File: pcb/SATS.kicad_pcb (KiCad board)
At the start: 2 copper layers, 108.5 x 103.4 mm, 27 parts, among them J1 Raspberry_Pi_2_3, J10 EXT_GPIO, J11 EXT_GPIO, J12 EXT_GPIO, J13 EXT_GPIO, J2 A00-432-262-450, J3 AudioJack4_SwitchTR1, J4 5V, J5 3.3V, J6 Card LED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

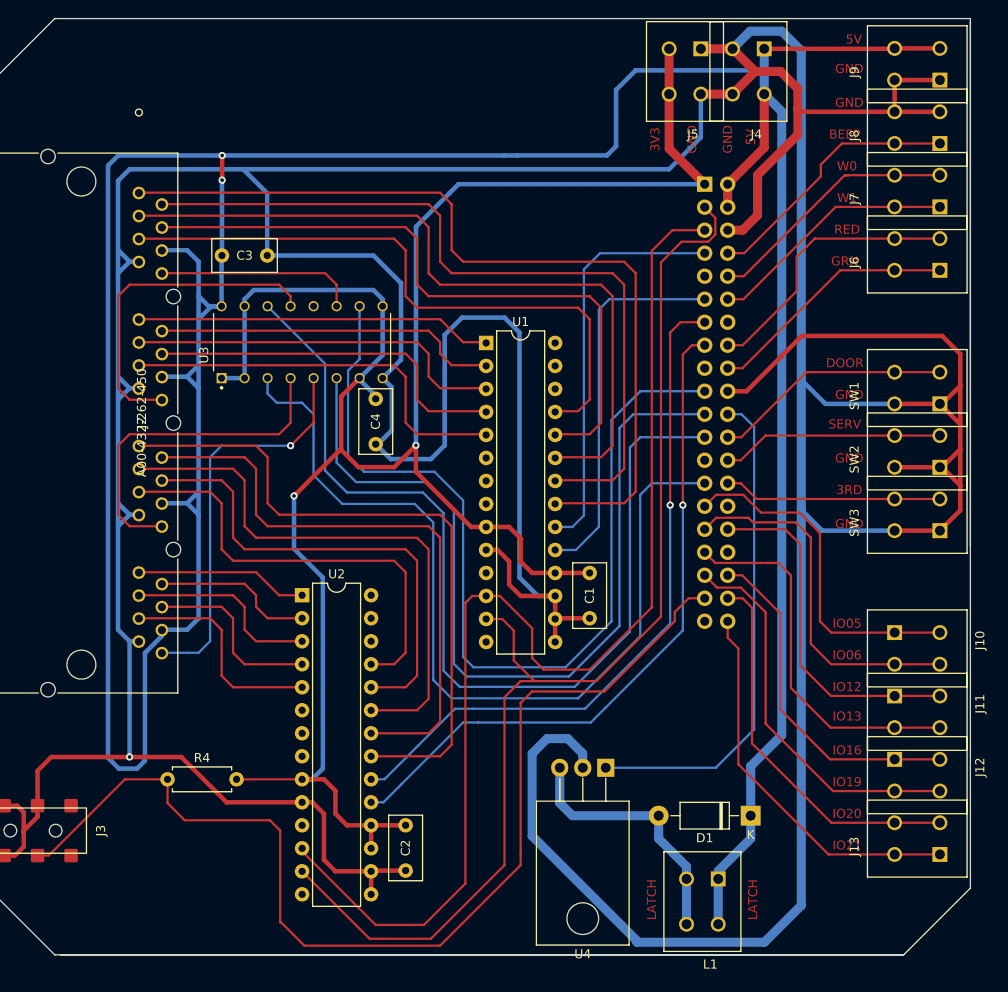
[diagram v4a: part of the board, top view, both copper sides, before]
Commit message: Clean Board Edge and Foottprints
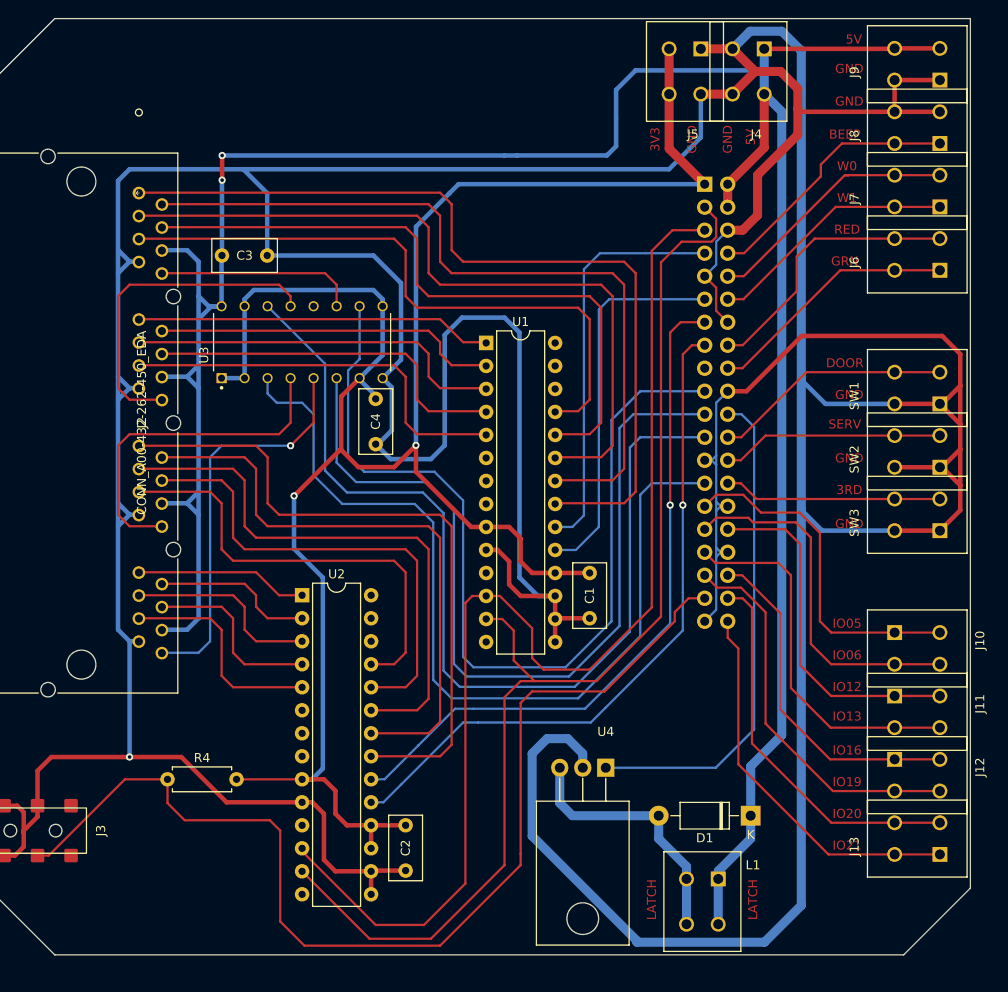
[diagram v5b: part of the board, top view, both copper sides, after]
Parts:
- J2: value A00-432-262-450 -> CONN_A00-432-262-450_EDA
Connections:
- J1 pad 17: +3V3 -> unconnected-(J1-Pad17)
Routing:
- net +5V: track 384.8 -> 286.2 mm
- net Earth: track 669.9 -> 715.2 mm
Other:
- outline, holes or cut-outs redrawn

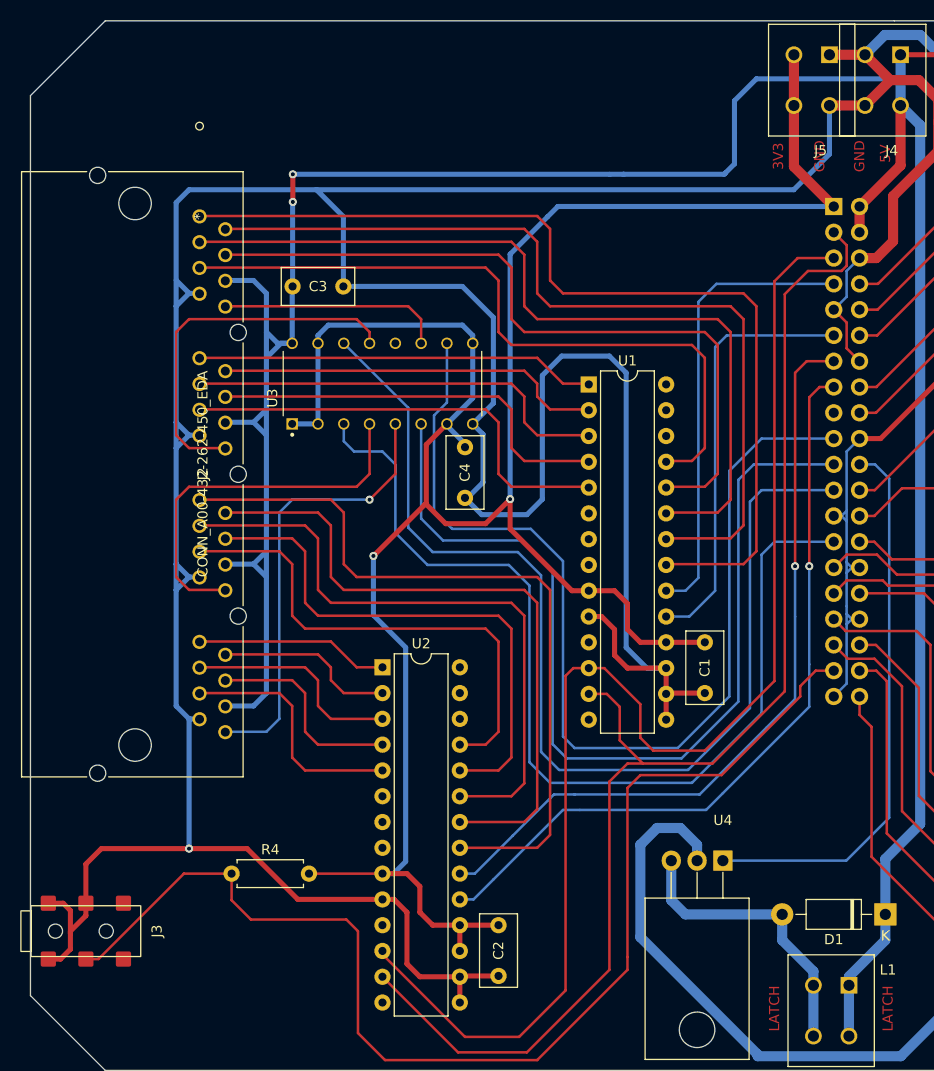
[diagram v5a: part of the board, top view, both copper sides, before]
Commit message: add copper labels
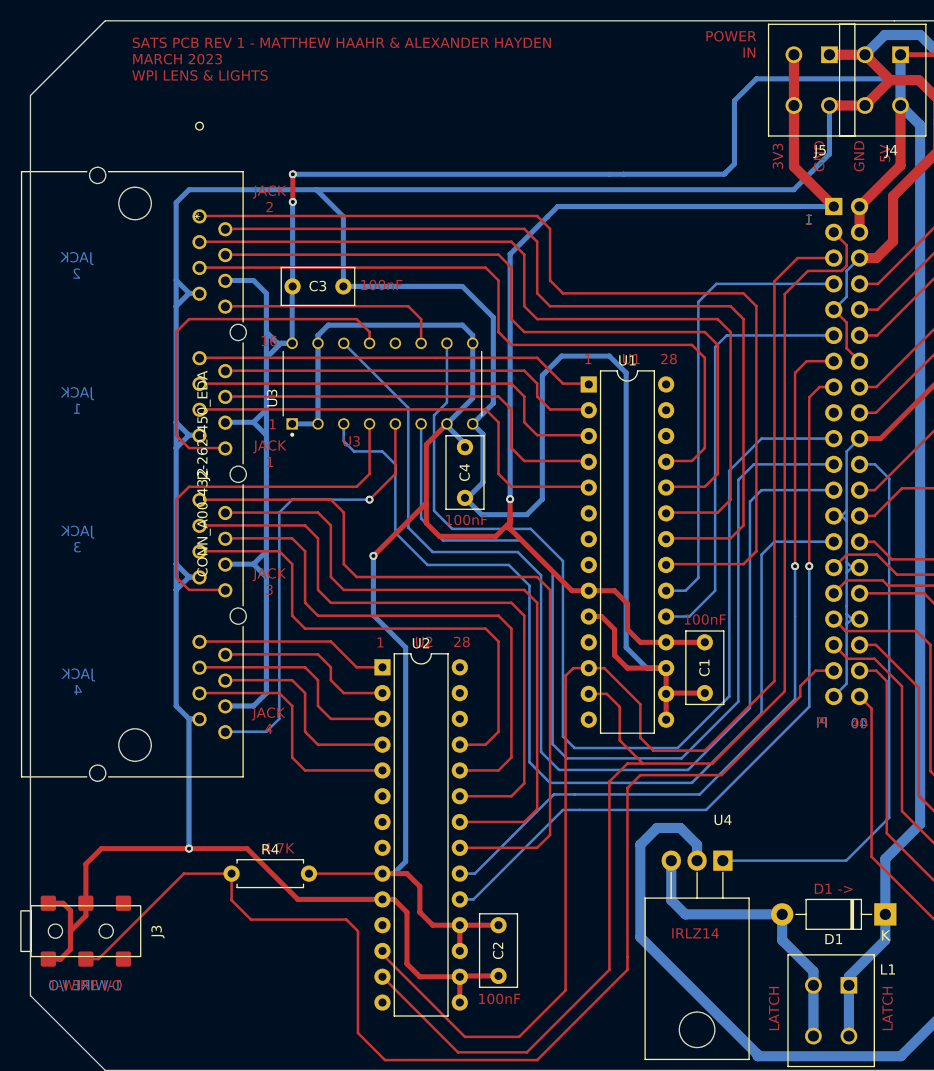
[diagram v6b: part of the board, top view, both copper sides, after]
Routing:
- net +3V3: track 228.0 -> 229.9 mm
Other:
- board text added: "1"
- board text added: "1-WIRE I/O"
- board text added: "100nF"
- board text added: "16"
- board text added: "28"
- board text added: "4.7K"
- board text added: "40"
- board text added: "D1 ->"
- board text added: "IRLZ14"
- board text added: "JACK 1"
- board text added: "JACK 2"
- board text added: "JACK 3"
- board text added: "JACK 4"
- board text added: "PI"
- board text added: "POWER IN"
- board text added: "SATS PCB REV 1 - MATTHEW HAAHR & ALEXANDER HAYDEN MARCH 2023 WPI LENS & LIGHTS"
- board text added: "U1"
- board text added: "U2"
- board text added: "U3"

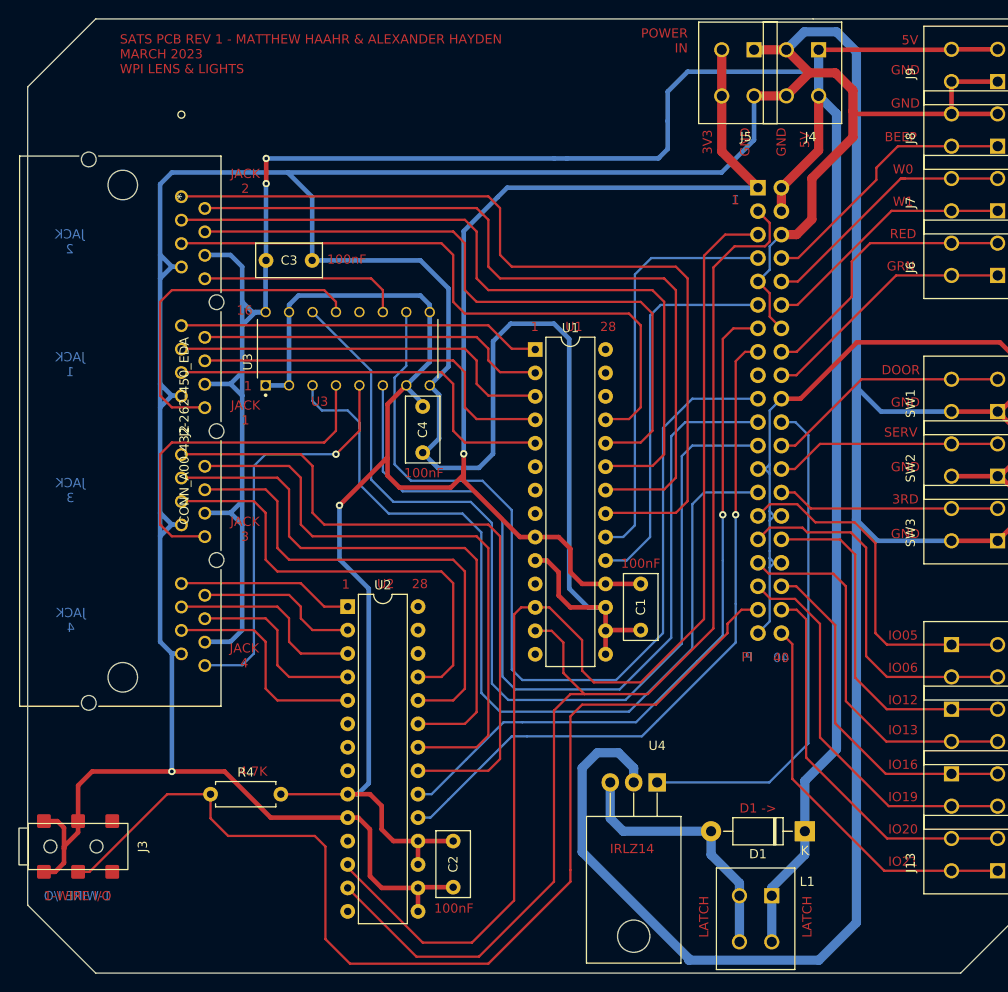
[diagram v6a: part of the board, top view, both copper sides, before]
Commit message: Add Mounting Holes and Fix Errors
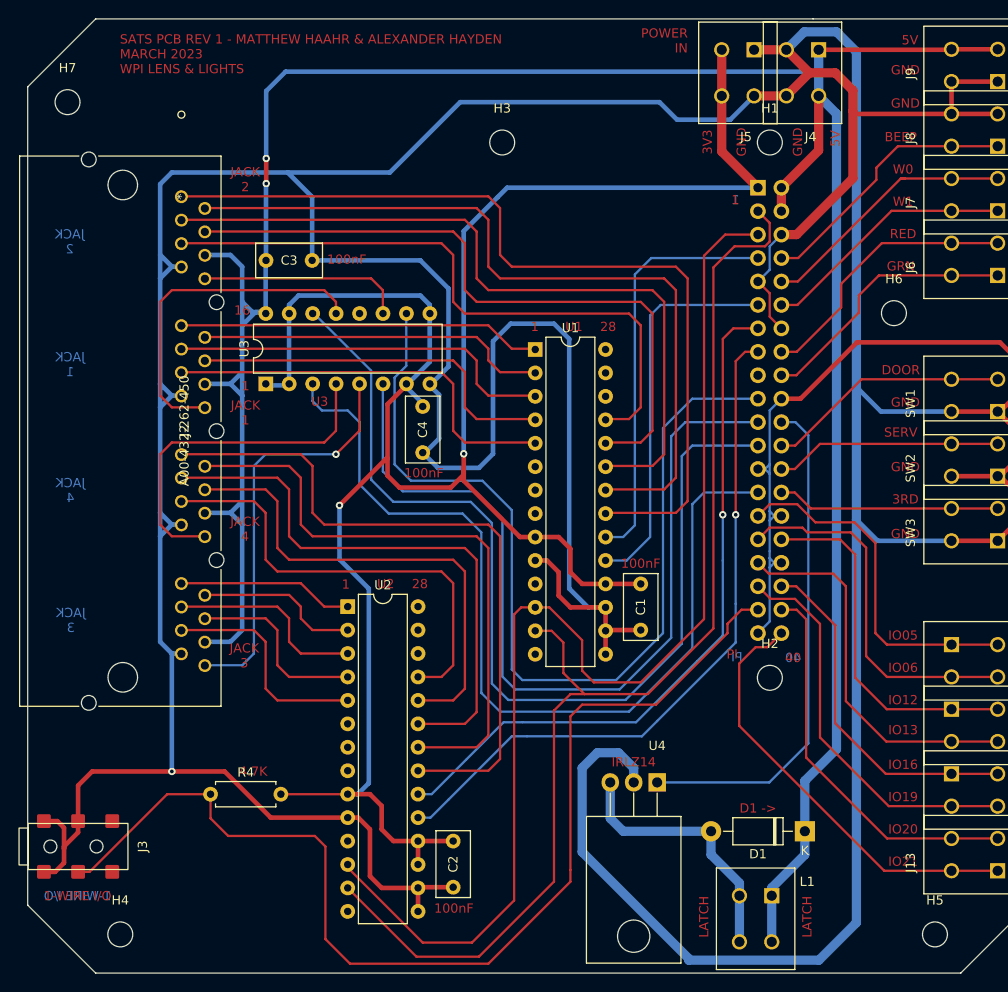
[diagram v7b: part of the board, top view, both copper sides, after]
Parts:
- added H1: MountingHole, MountingHole:MountingHole_2.7mm_M2.5, F.Cu at (130.1, 58.3)
- added H2: MountingHole, MountingHole:MountingHole_2.7mm_M2.5, F.Cu at (130.1, 116.3)
- added H3: MountingHole, MountingHole:MountingHole_2.7mm_M2.5, F.Cu at (101.1, 58.3)
- added H4: MountingHole, MountingHole:MountingHole_2.7mm_M2.5, F.Cu at (59.7, 144.1)
- added H5: MountingHole, MountingHole:MountingHole_2.7mm_M2.5, F.Cu at (148.0, 144.1)
- added H6: MountingHole, MountingHole:MountingHole_2.7mm_M2.5, F.Cu at (143.5, 76.8)
- added H7: MountingHole, MountingHole:MountingHole_2.7mm_M2.5, F.Cu at (54.0, 54.0)
- J2: value CONN_A00-432-262-450_EDA -> A00-432-262-450
- U3: footprint CD40109BE:DIP794W45P254L1969H508Q16 -> Package_DIP:DIP-16_W7.62mm
- moved U3 9.66 mm to (75.5, 84.5)
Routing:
- net EXT_GPIO21: track 42.7 -> 47.2 mm
- net Earth: track 715.2 -> 714.0 mm
- net Card GRN: track 27.9 -> 29.0 mm
- net Card RED: track 30.5 -> 29.8 mm
- net +5V: track 286.2 -> 286.8 mm

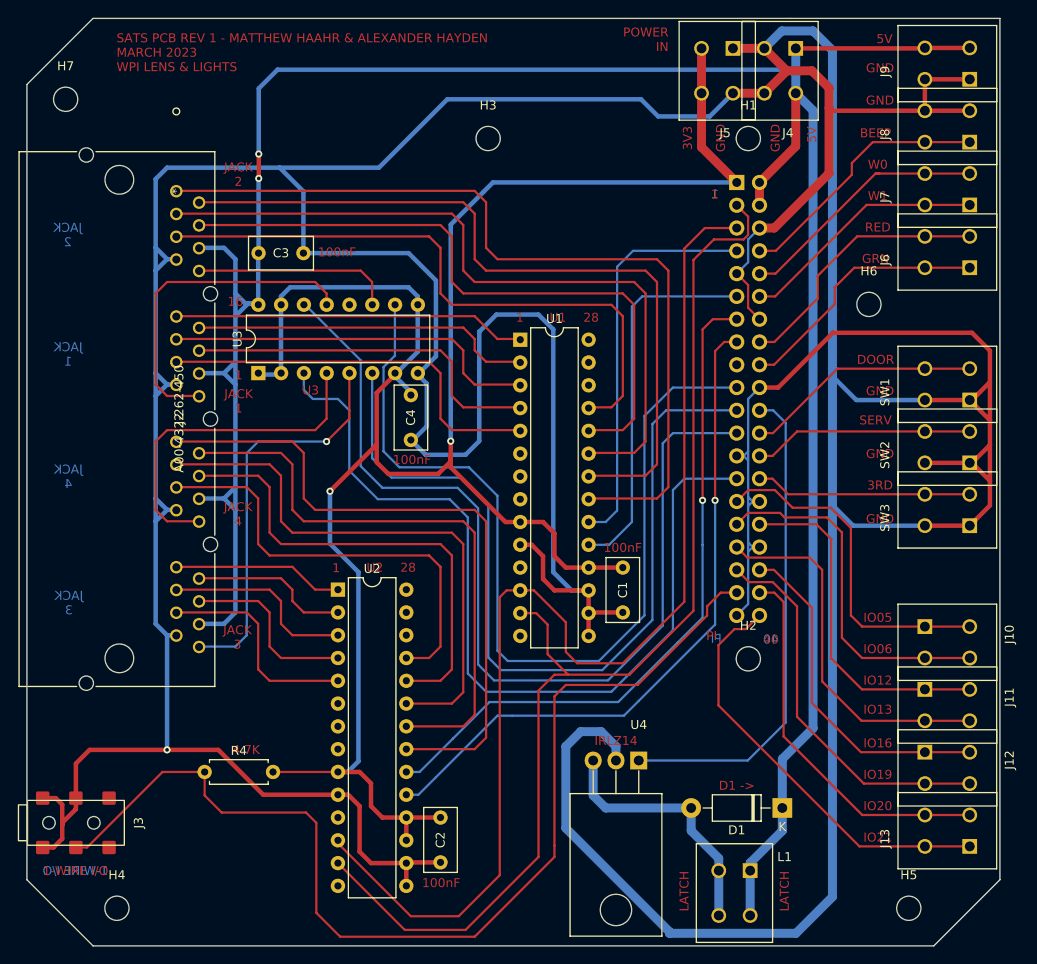
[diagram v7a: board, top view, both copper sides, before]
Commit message: Added <no-net> Copper Fills
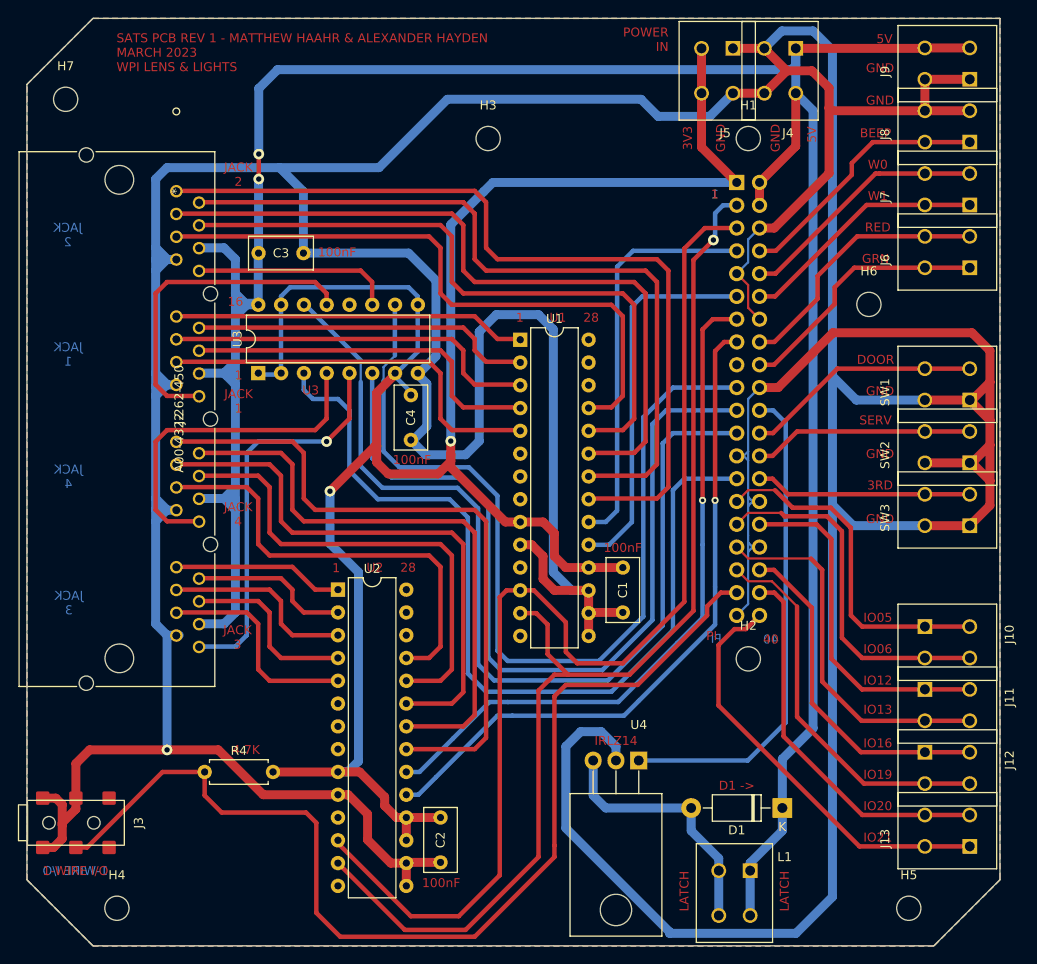
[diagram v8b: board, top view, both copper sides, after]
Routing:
- net +5V: track 286.8 -> 292.9 mm
- net SDA: track 128.6 -> 126.6 mm, vias 0 -> 1
- net Earth: track 714.0 -> 715.7 mm
- net +3V3: track 229.9 -> 229.0 mm
- added copper zone on B.Cu, net (none)
- added copper zone on F.Cu, net (none)
